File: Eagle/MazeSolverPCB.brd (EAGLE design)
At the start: 53.3 x 50.8 mm, 26 parts

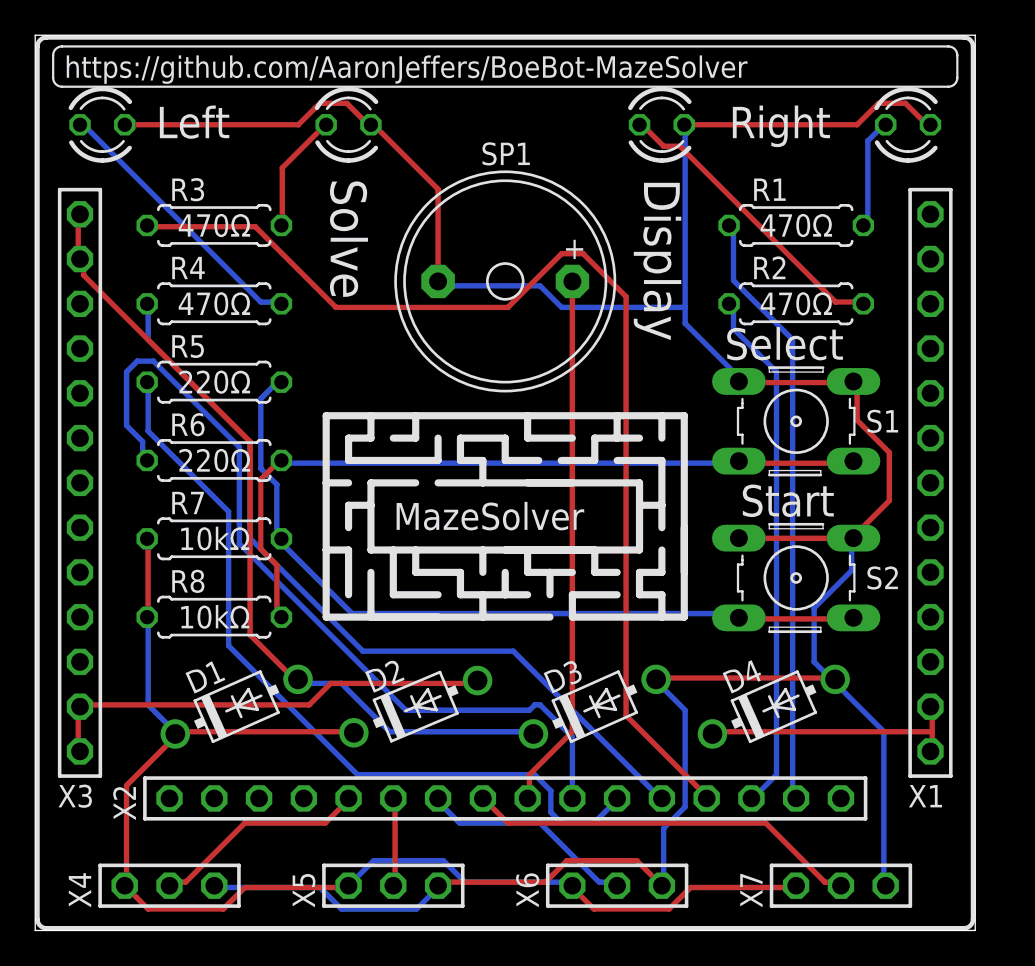
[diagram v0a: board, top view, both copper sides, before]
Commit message: Changed Autorouting
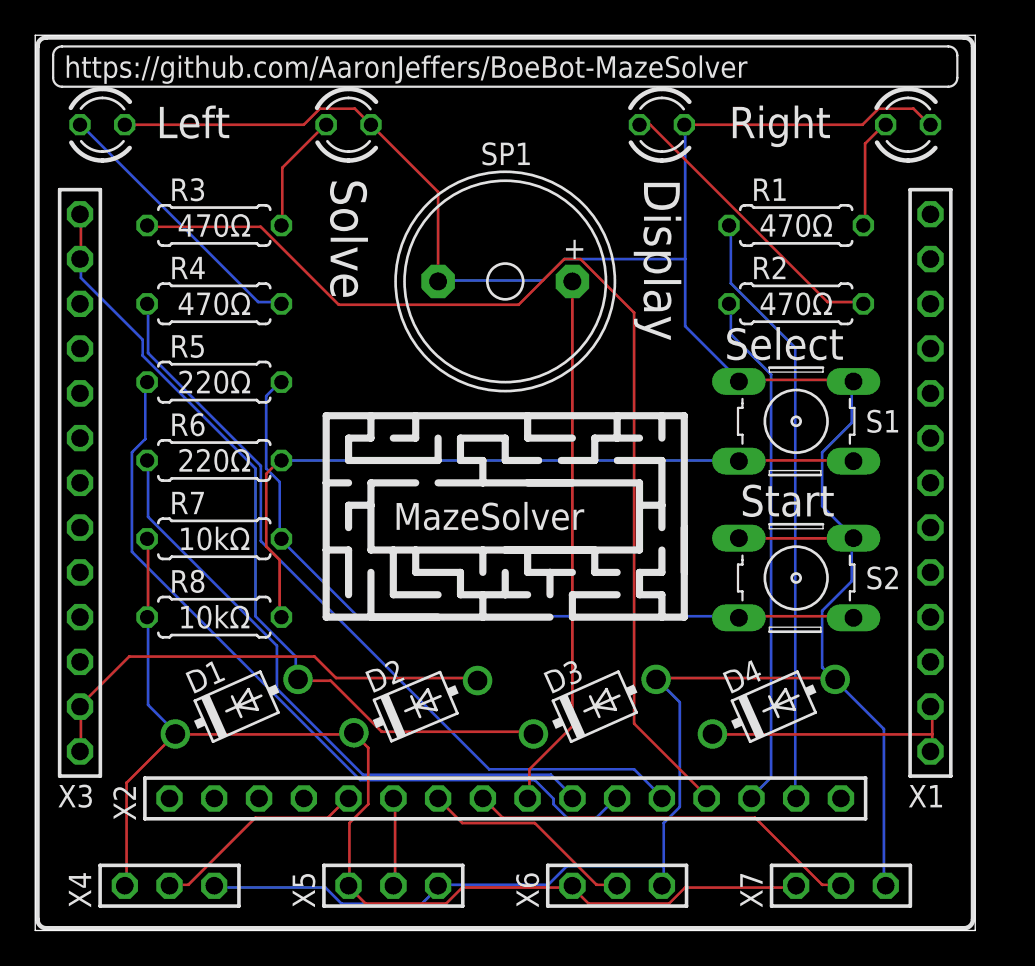
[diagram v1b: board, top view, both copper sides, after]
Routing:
- net N$27: track 46.9 -> 35.5 mm
- net N$2: track 73.3 -> 68.4 mm
- net N$1: track 168.3 -> 165.8 mm
- net N$15: track 25.8 -> 26.9 mm
- net N$6: track 61.8 -> 61.1 mm
- net N$12: track 44.8 -> 44.2 mm
- net N$13: track 42.8 -> 42.2 mm
